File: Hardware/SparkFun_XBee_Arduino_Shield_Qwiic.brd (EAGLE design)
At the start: 53.3 x 59.7 mm, 156 parts, among them J4 QWIIC_RIGHT_ANGLE, U1 FSUSB30MUX_MSOP10, U2 AP63203, U3 ESD Diode, U4 FT231XS, U5 ESD Diode, U6 TXS0108, U7 TXS0108

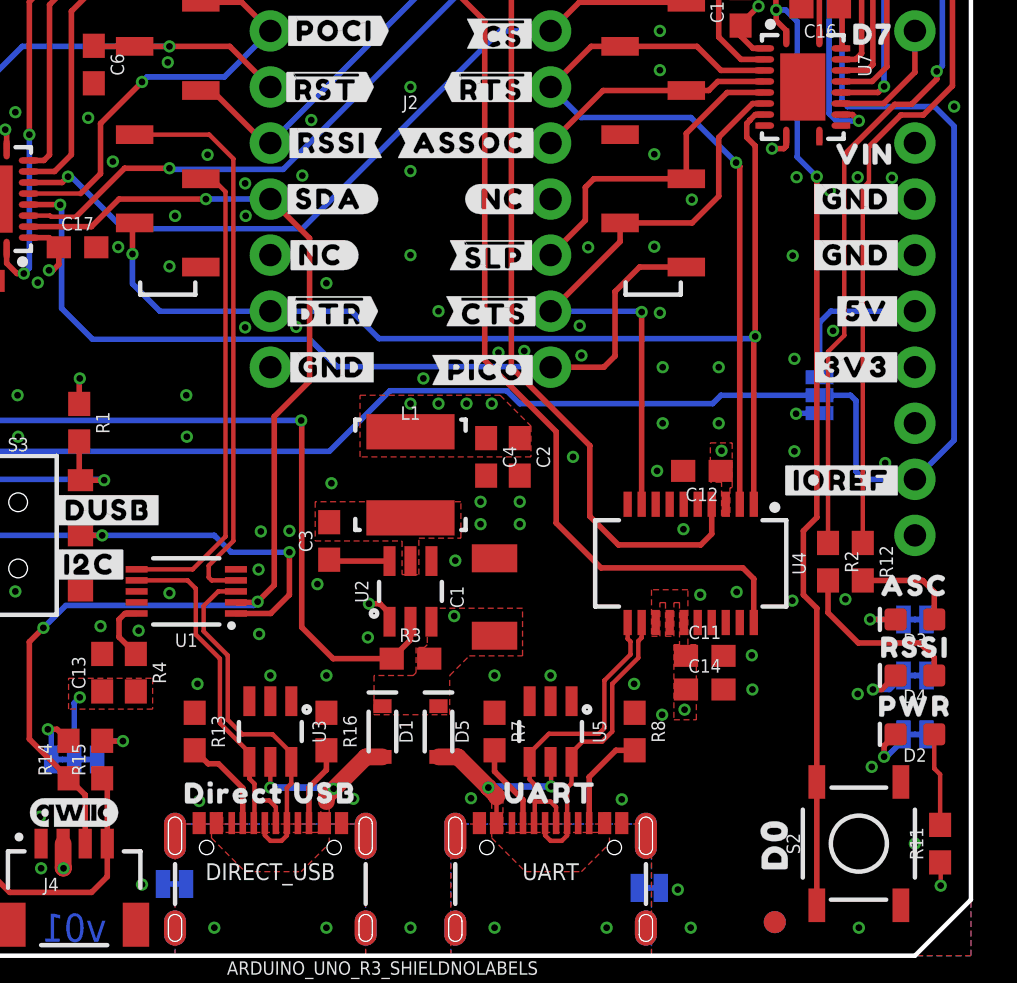
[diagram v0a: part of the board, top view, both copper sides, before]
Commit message: Adds "1, 2, 3, 4" to layers and special ordering instructions
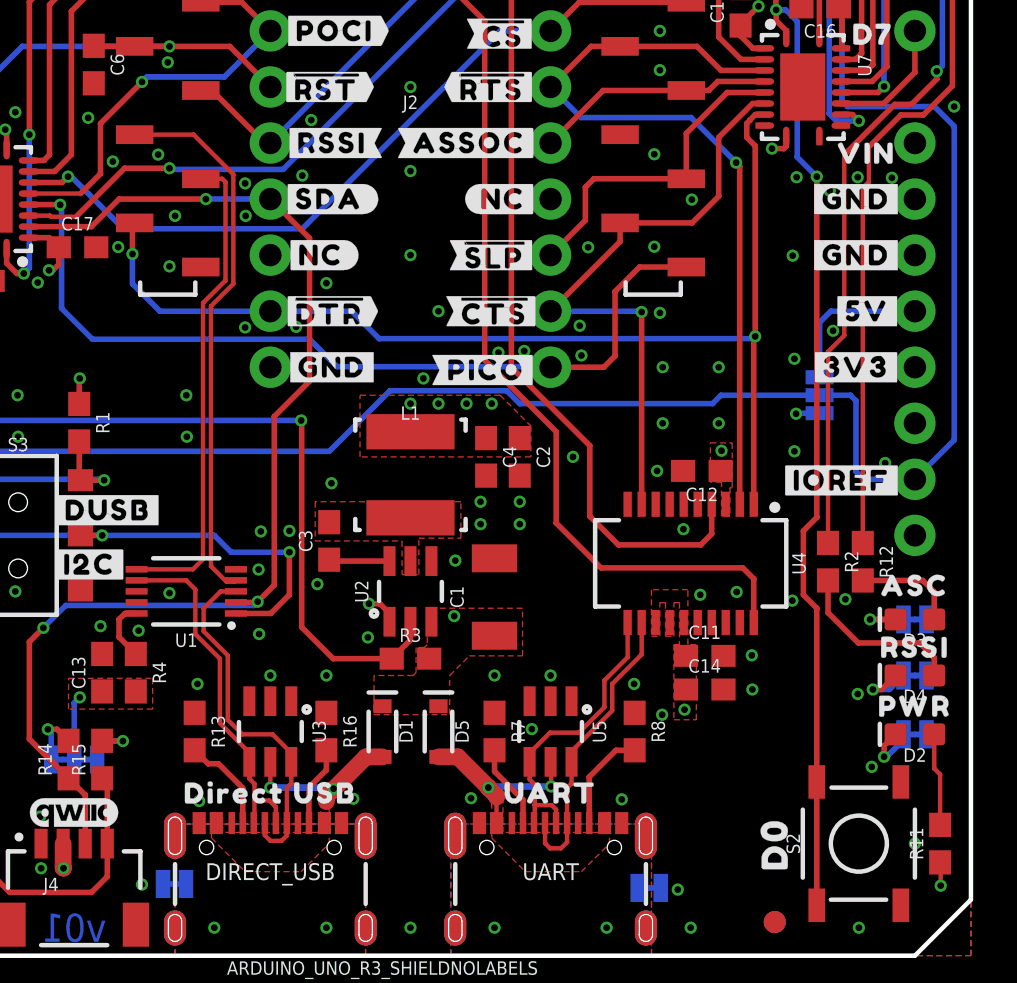
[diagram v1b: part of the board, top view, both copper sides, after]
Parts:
- moved U$66 0.08 mm to (48.6, 36.4)
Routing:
- net XBEE_D+/SDA: track 25.7 -> 24.8 mm
- net D-: track 14.3 -> 13.5 mm

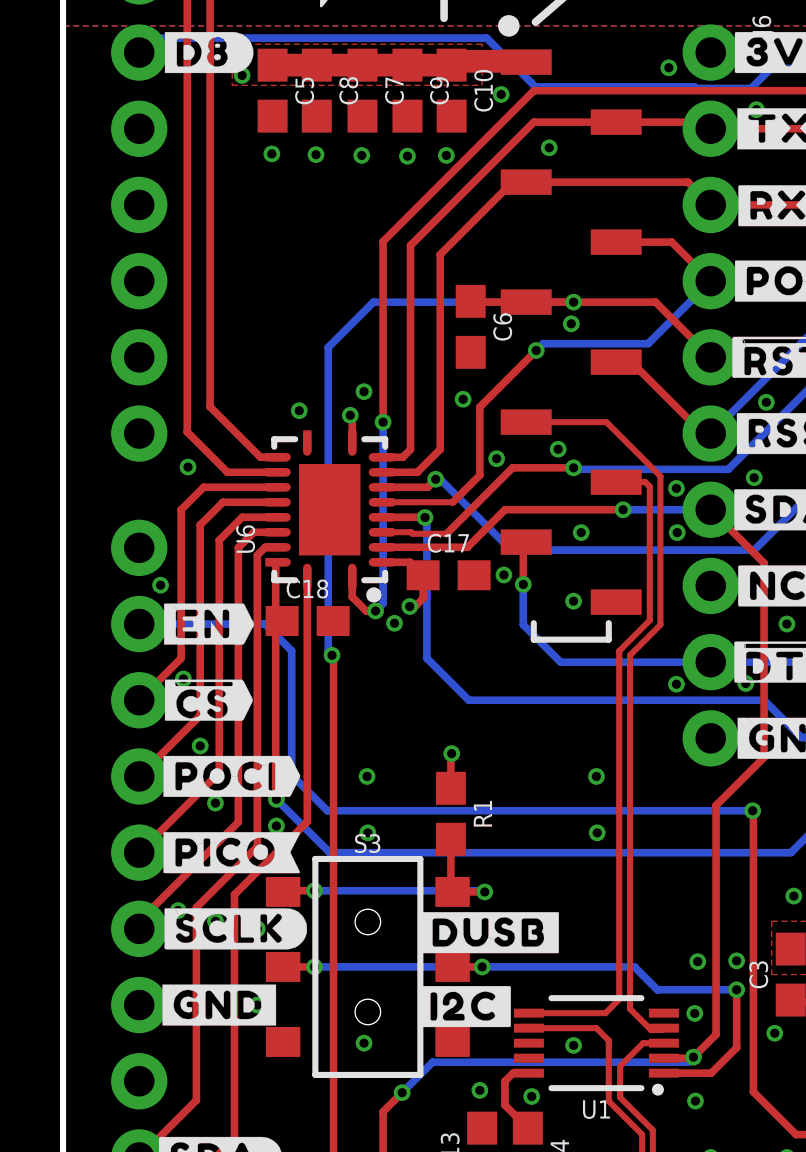
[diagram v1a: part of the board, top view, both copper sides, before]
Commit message: Fixes wire stub DRC error
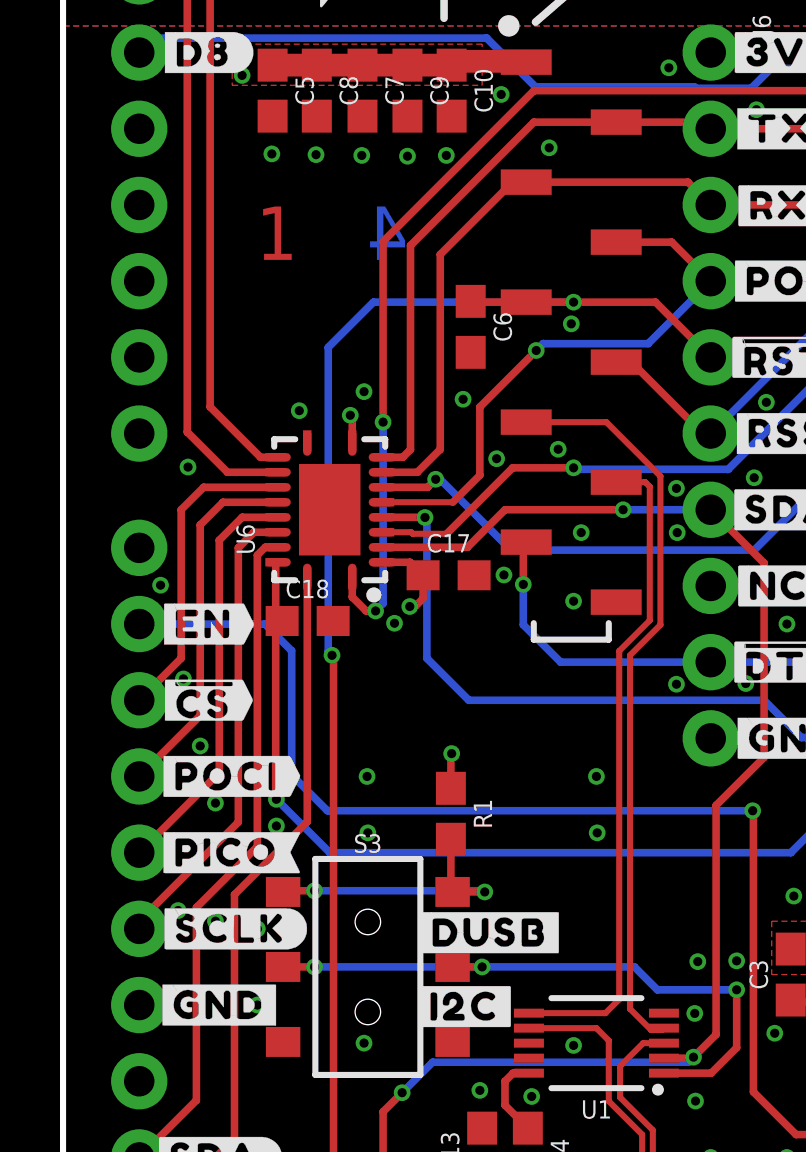
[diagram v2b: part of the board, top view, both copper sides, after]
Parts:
- added LOGO4: SPECIAL_INSTRUCTIONS-ORDERING, SparkFun-Aesthetics:ORDERING_INSTRUCTIONS
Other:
- board text added: "1"
- board text added: "1.6mm Thickness"
- board text added: "2"
- board text added: "3"
- board text added: "4"
- board text added: "Four Layer Board"
- board text added: "Lead Free HASL"
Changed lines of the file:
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@@
 <layer number="27" name="tValues" color="7" fill="1" visible="no" active="yes"/>
 <layer number="28" name="bValues" color="7" fill="1" visible="no" active="yes"/>
-<layer number="29" name="tStop" color="7" fill="3" visible="yes" active="yes"/>
+<layer number="29" name="tStop" color="7" fill="3" visible="no" active="yes"/>
 <layer number="30" name="bStop" color="7" fill="6" visible="no" active="yes"/>
 <layer number="31" name="tCream" color="7" fill="4" visible="no" active="yes"/>
@@
 <layer number="37" name="tTest" color="7" fill="1" visible="no" active="yes"/>
 <layer number="38" name="bTest" color="7" fill="1" visible="no" active="yes"/>
-<layer number="39" name="tKeepout" color="4" fill="11" visible="yes" active="yes"/>
+<layer number="39" name="tKeepout" color="4" fill="11" visible="no" active="yes"/>
 <layer number="40" name="bKeepout" color="1" fill="11" visible="no" active="yes"/>
 <layer number="41" name="tRestrict" color="4" fill="10" visible="no" active="yes"/>
@@
 <text x="-21.59" y="-6.35" size="1.778" layer="47" font="vector">Units in Inches</text>
 <rectangle x1="11.049" y1="36.3728" x2="11.176" y2="36.9062" layer="41"/>
+<text x="6.428" y="42.619" size="1.778" layer="1" font="vector" ratio="15">1</text>
+<text x="7.698" y="42.619" size="1.778" layer="2" font="vector" ratio="15">2</text>
+<text x="8.968" y="42.619" size="1.778" layer="15" font="vector" ratio="15">3</text>
+<text x="11.508" y="42.619" size="1.778" layer="16" font="vector" ratio="15" rot="SMR0">4</text>
+<text x="60.5" y="44.5" size="1.778" layer="51" font="vector" ratio="15">Four Layer Board</text>
+<text x="60.5" y="41" size="1.778" layer="51" font="vector" ratio="15">1.6mm Thickness</text>
+<text x="60.5" y="37.5" size="1.778" layer="51" font="vector" ratio="15">Lead Free HASL</text>
 </plain>
 <attributes>
@@
 <element name="U$89" library="bot" package="#IOREF#35" value="" x="48.26" y="25.4" smashed="yes" rot="MR90"/>
 <element name="U$66" library="top" package="VIN5" value="" x="48.6094" y="36.362" smashed="yes"/>
+<element name="LOGO4" library="SparkFun-Aesthetics" package="ORDERING_INSTRUCTIONS" value="SPECIAL_INSTRUCTIONS-ORDERING" x="58" y="56.5" smashed="yes"/>
 </elements>
 <signals>
@@
 <contactref element="S3" pad="5"/>
 <contactref element="S3" pad="2"/>
-<wire x1="12.9342" y1="18.9992" x2="12.985" y2="19.05" width="0.254" layer="1"/>
 <wire x1="20.03" y1="15.51" x2="21.606" y2="15.51" width="0.254" layer="1"/>
 <wire x1="22.4536" y1="18.288" x2="22.4536" y2="16.3576" width="0.254" layer="1"/>

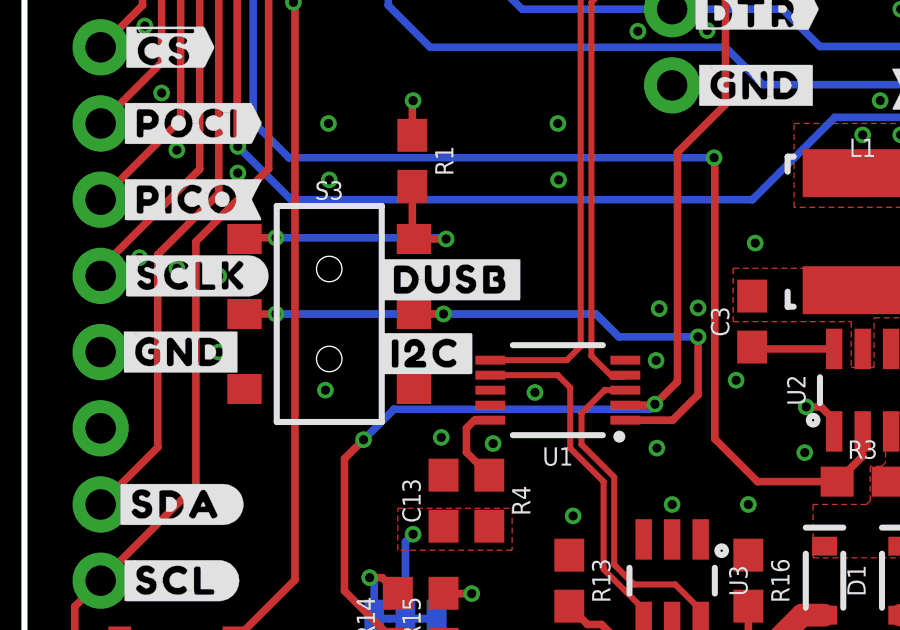
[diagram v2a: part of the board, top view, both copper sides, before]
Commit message: Adjusts two silk labels ever so slightly
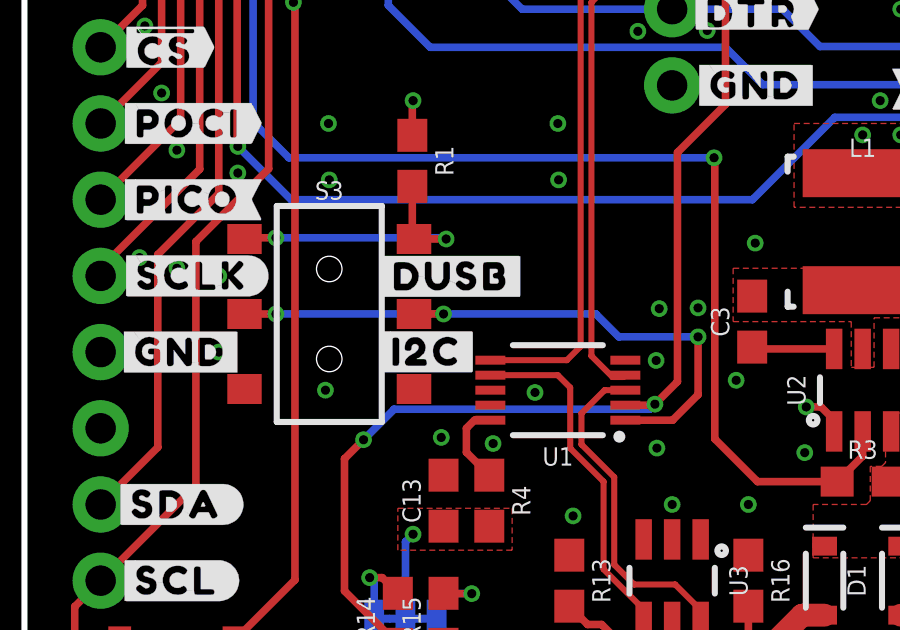
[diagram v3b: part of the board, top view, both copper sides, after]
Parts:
- moved U$72 0.11 mm to (14.2, 20.3)
- moved U$73 0.06 mm to (13.4, 17.8)
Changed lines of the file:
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@@
 <element name="U$70" library="top" package="#PICO#24" value="" x="31.369" y="26.543" smashed="yes"/>
 <element name="U$71" library="topmirror" package="DIRECT_USB33" value="" x="21.59" y="7.366" smashed="yes"/>
-<element name="U$72" library="botmirror" package="#DUSB#31" value="" x="14.224" y="20.193" smashed="yes"/>
+<element name="U$72" library="botmirror" package="#DUSB#31" value="" x="14.224" y="20.303" smashed="yes"/>
 <element name="U$74" library="top" package="ASC32" value="" x="50.8" y="16.764" smashed="yes"/>
 <element name="U$1" library="top" package="RSSI31" value="" x="50.8" y="13.97" smashed="yes"/>
@@
 </element>
 <element name="U$83" library="top" package="D727" value="" x="48.9204" y="41.7576" smashed="yes"/>
-<element name="U$73" library="top" package="#I2C#13751" value="" x="13.3858" y="17.7292" smashed="yes"/>
+<element name="U$73" library="top" package="#I2C#13751" value="" x="13.4058" y="17.7892" smashed="yes"/>
 <element name="LOGO1" library="SparkFun-Aesthetics" package="BLANK" value="SFE_LOGO_NAMEBLANK" x="-30.48" y="-38.1" smashed="yes"/>
 <element name="U$88" library="top" package="#IOREF#6" value="" x="47.4726" y="21.5392" smashed="yes"/>

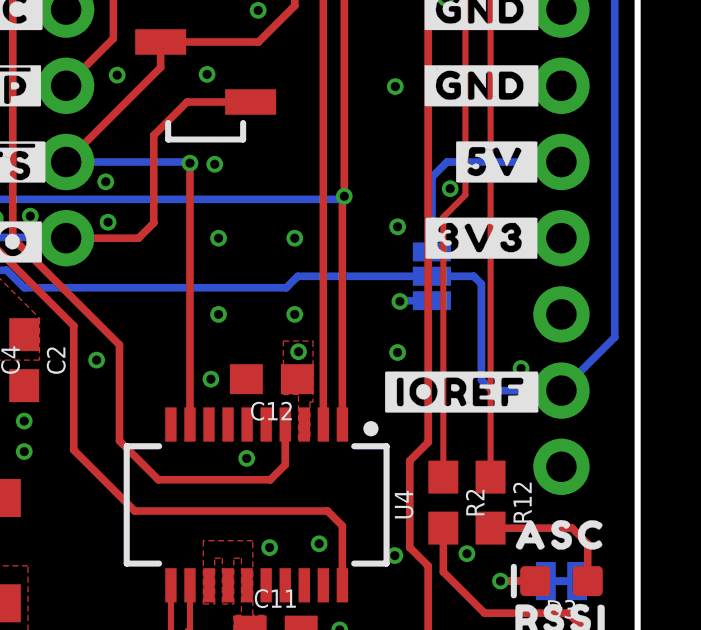
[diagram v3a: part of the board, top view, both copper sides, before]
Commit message: Adds protos
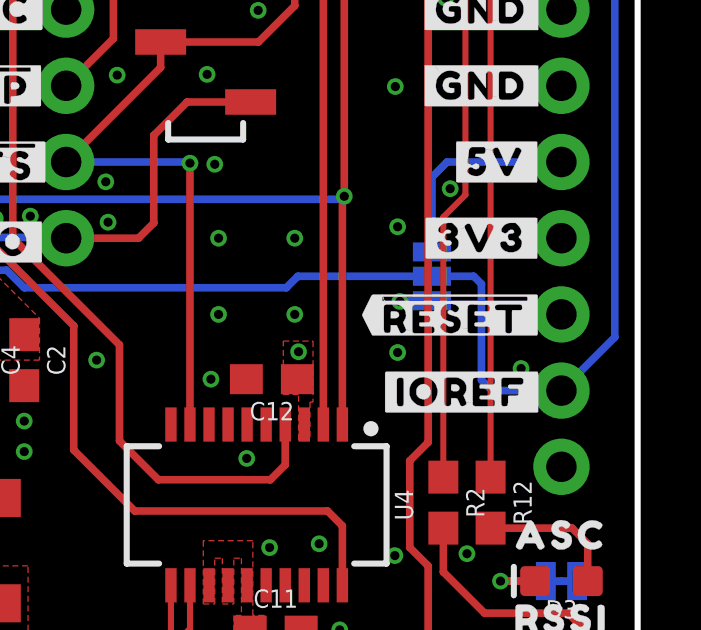
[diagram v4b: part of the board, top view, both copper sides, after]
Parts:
- added U$87: (no value), top:##RESET##23
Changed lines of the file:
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@@
 <element name="U$66" library="top" package="VIN5" value="" x="48.6094" y="36.362" smashed="yes"/>
 <element name="LOGO4" library="SparkFun-Aesthetics" package="ORDERING_INSTRUCTIONS" value="SPECIAL_INSTRUCTIONS-ORDERING" x="58" y="56.5" smashed="yes"/>
+<element name="U$87" library="top" package="##RESET##23" value="" x="47.25" y="24.11" smashed="yes"/>
 </elements>
 <signals>

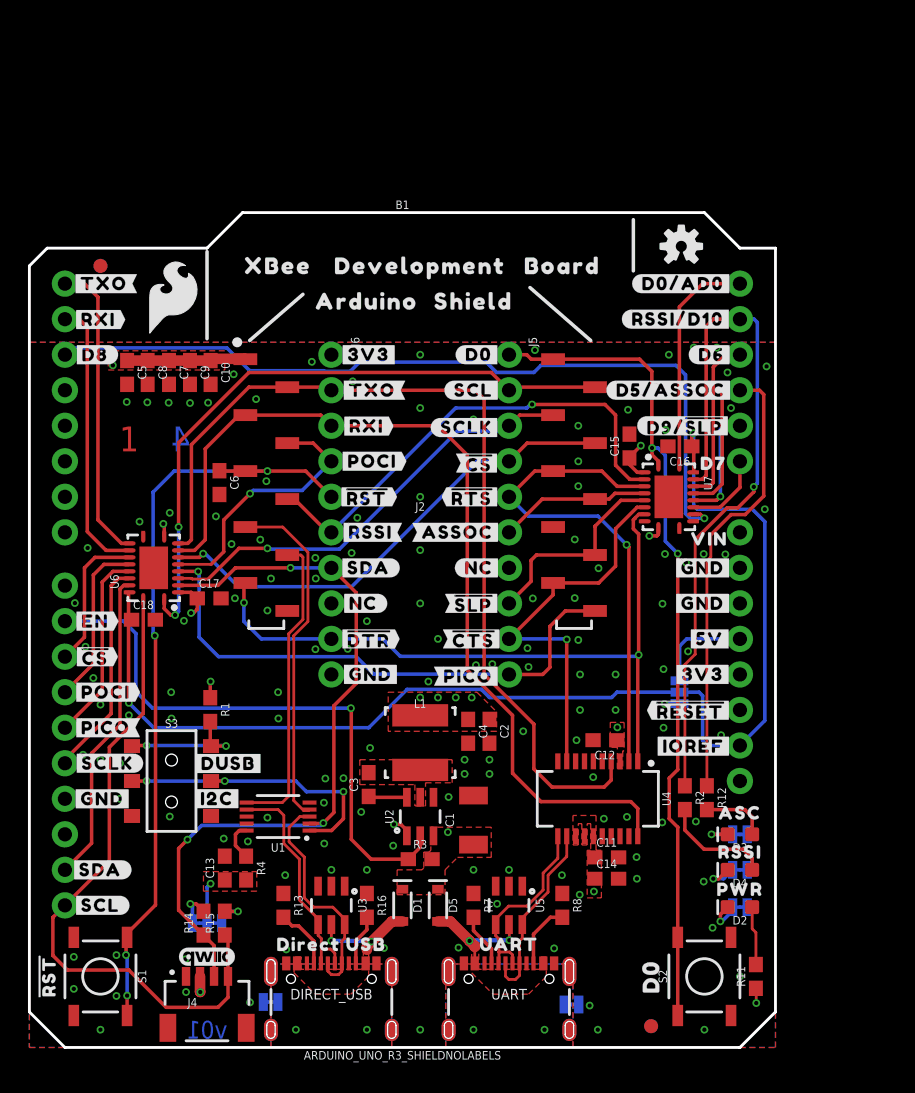
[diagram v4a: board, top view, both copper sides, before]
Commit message: Rolls to v02
* Fixes USB data lines on main UART
* Shifts ASC, RSSI nets to LEDs to be non-translated by default
* Move SCL data line to non-translated by default
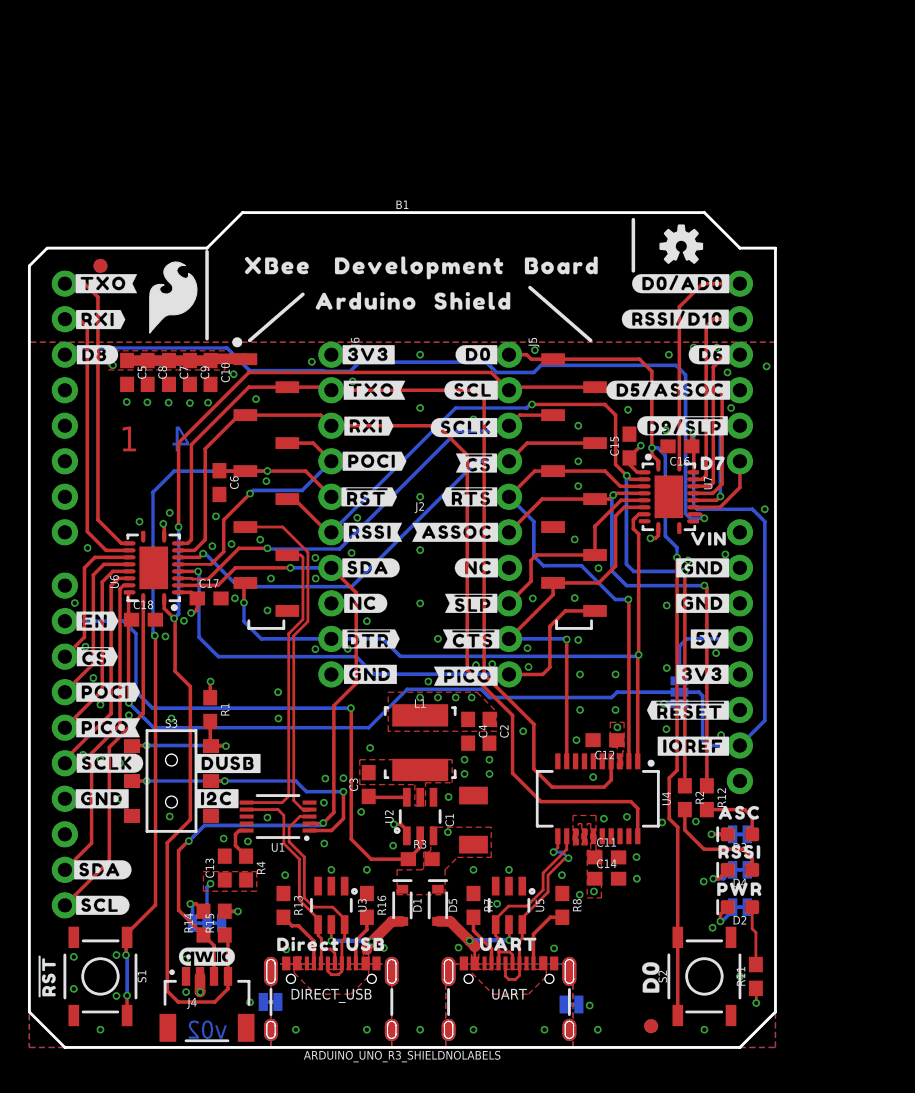
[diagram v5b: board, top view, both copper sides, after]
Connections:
- net D+: now also U4.11; no longer U4.12
- net D-: now also U4.12; no longer U4.11
- net D1/SCL: now also J4.4, R15.1
- net D1/SCL-TRANS: no longer J4.4, R15.1
- net D10/RSSI_PWM: now also R2.1
- net D10/RSSI_PWM-TRANS: no longer R2.1
- net D5/ASSOCIATE: now also R12.1
- net D5/ASSOCIATE-TRANS: no longer R12.1
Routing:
- net D1/SCL: track 46.5 -> 83.6 mm
- net D10/RSSI_PWM-TRANS: track 51.3 -> 14.3 mm, vias 1 -> 0
- net D5/ASSOCIATE-TRANS: track 42.2 -> 10.1 mm
- net D5/ASSOCIATE: track 10.8 -> 37.7 mm, vias 0 -> 2
- net D10/RSSI_PWM: track 34.6 -> 60.6 mm, vias 1 -> 3
- net D1/SCL-TRANS: track 47.0 -> 24.1 mm
- net D+: track 13.5 -> 14.6 mm, vias 0 -> 2
- net D6/!RTS!: track 36.2 -> 35.4 mm
- net D7/!CTS!: track 28.4 -> 29.0 mm
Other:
- board text added: "v02"
- board text removed: "v01"
